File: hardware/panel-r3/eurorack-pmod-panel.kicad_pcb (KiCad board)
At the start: 2 copper layers, 15 x 128.5 mm, 11 parts

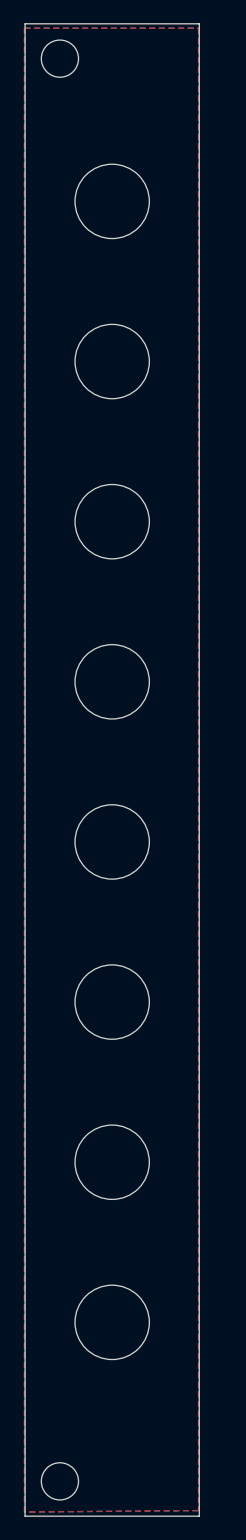
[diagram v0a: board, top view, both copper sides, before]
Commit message: rev3/panel: fix slots, circles on nuts
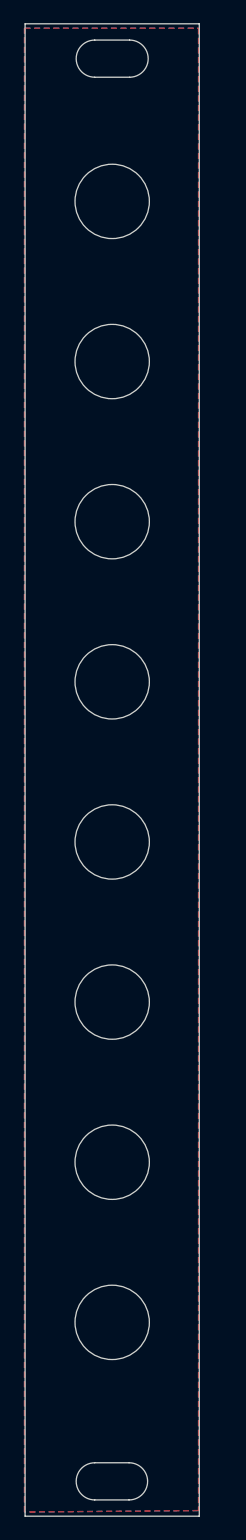
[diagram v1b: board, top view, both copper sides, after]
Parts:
- removed the REF** at (0.00, 3.00)
- removed the REF** at (0.00, 125.5)
- added kibuzzard-641AEA5C: G***, kibuzzard-641AEA5C, F.Cu at (4.45, 7.45)
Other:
- outline, holes or cut-outs redrawn
- board text added: "///////"
- board text added: "α"
- board text added: "β"
- board text added: "γ"
- board text added: "δ"
- board text removed: "/////////"
- board text removed: "/vk2"
- board text removed: "0"
- board text removed: "1"
- board text removed: "2"
- board text removed: "3"
- board text removed: "EURO"
- board text removed: "INPUTS"
- board text removed: "OUTPUTS"
- board text removed: "PMOD"

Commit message: rev3/panel: finish R3.1 panel, add fab outputs
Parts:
- removed kibuzzard-641AEA5C: G***, kibuzzard-641AEA5C
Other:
- board text added: "EURORACK"
- board text added: "PMOD"
- board text added: "UID: DE000135"
- board text added: "oshwa.org certified"
- board text added: "sebholzapfel.com"

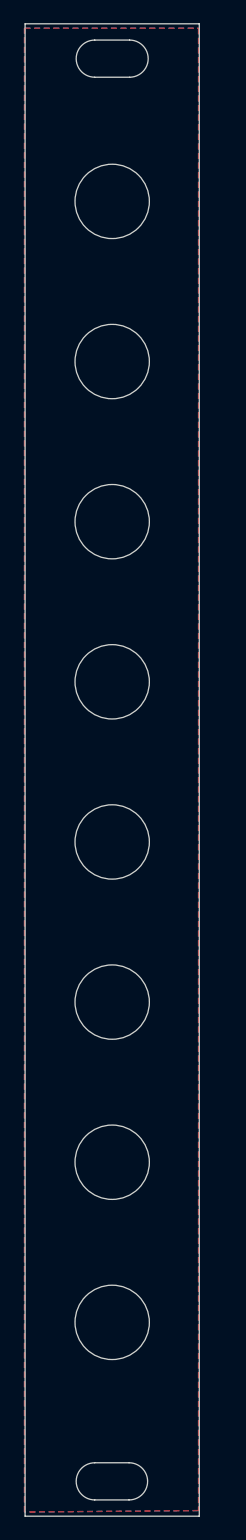
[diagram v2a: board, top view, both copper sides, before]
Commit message: panel: update for R3.3
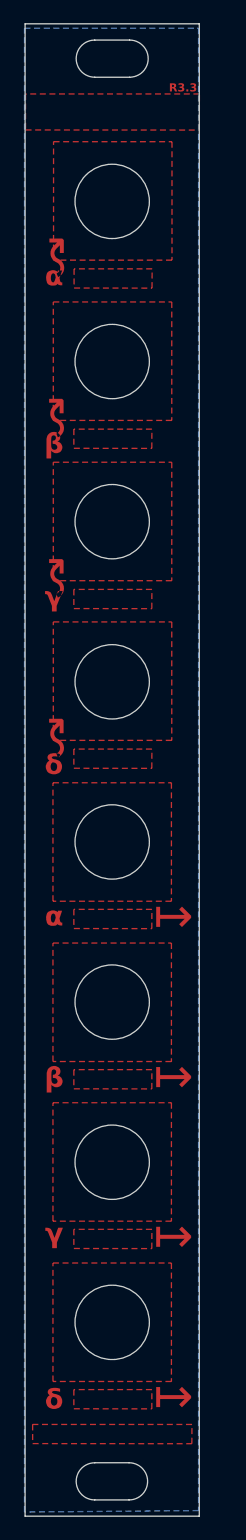
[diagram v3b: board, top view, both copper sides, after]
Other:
- board text added: "R3.3"
- board text added: "eurorack//"
- board text added: "pmod"
- board text added: "↝"
- board text added: "↦"
- board text removed: "EURORACK"
- board text removed: "PMOD"
- board text removed: "R3"
